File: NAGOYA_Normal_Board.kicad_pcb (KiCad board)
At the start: 2 copper layers, 60 x 71 mm, 104 parts, among them CN1 XT30-M, CN13 value, CN14 RefereeSystem, CN15 micro_B, CN2 XT30-M, CN3 XT30-F, CN4 XT30-F, CN5 XT30-F, CN6 XT30-F, J1 debug, J10 CAN3, J13 CAN3, J14 CAN3, J5 CAN3, J6 CAN3, J7 CAN3, J8 CAN3, J9 CAN3, Q2 DDTC114EUA-7-F, Q4 DDTC114EUA-7-F, Q5 DDTC114EUA-7-F, Q6 DDTC114EUA-7-F, SW1 SW_DIP_x04, U1 Teensy4.1, U2 TCAN1042HVDR, U3 TCAN1042HVDR, U4 TCAN1042HVDR, U5 FT234XD, U6 TLP172AM, U7 BNO055, U8 ADuM121N, U9 LXES11DAA2-137, Y2 32.768 k

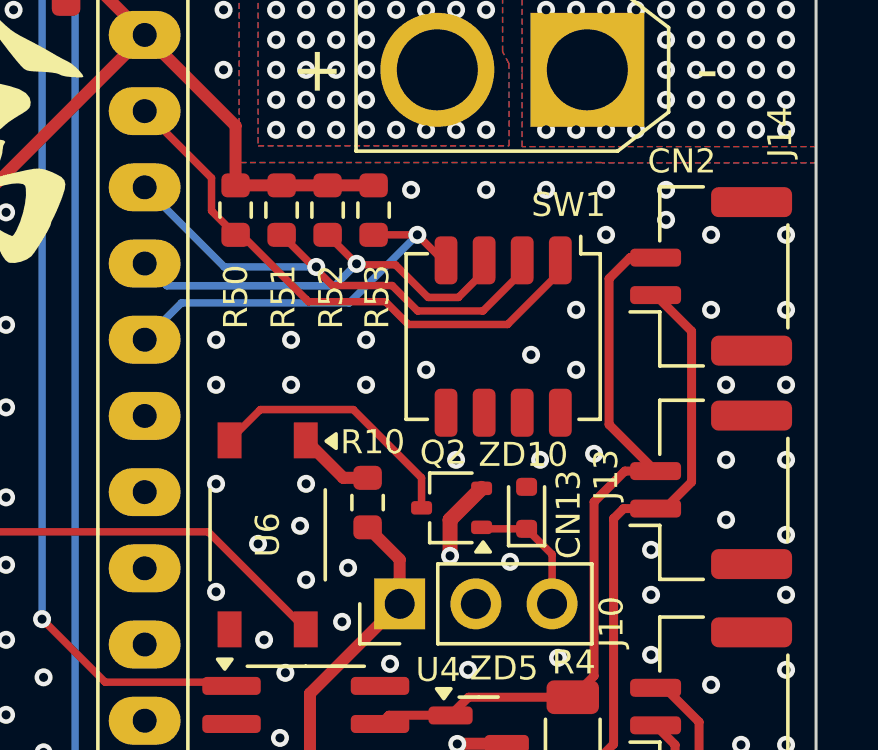
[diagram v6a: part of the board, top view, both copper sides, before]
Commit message: 発注用parameterを変更
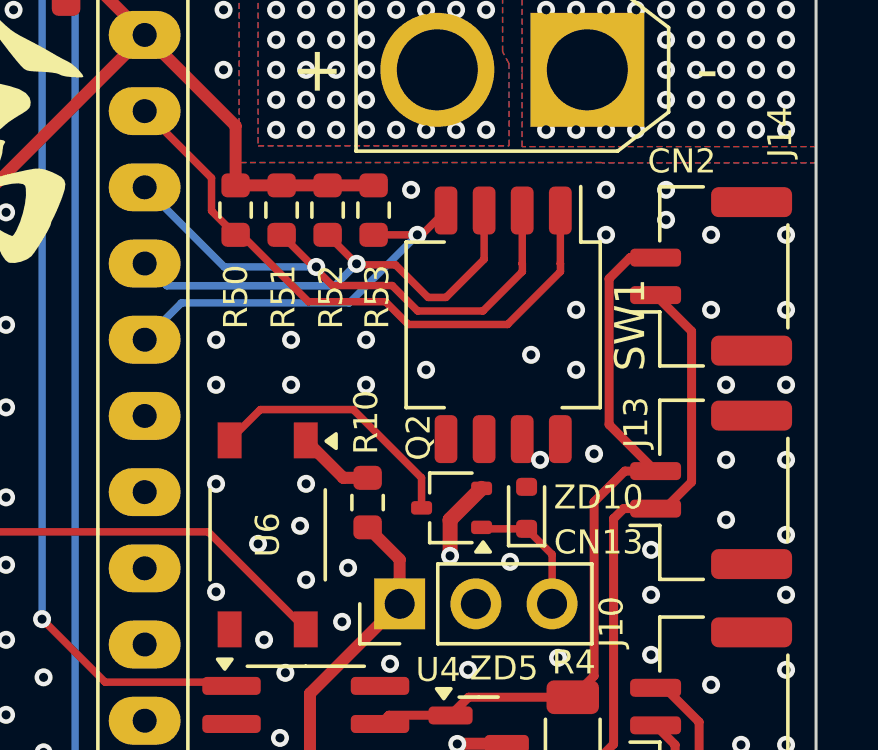
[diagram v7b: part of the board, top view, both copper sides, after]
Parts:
- SW1: footprint Button_Switch_SMD:SW_DIP_SPSTx04_Slide_Copal_CHS-04A_W5.08mm_P1.27mm_JPin -> Button_Switch_SMD:SW_DIP_SPSTx04_Slide_Copal_CHS-04B_W7.62mm_P1.27mm
- moved SW1 0.39 mm to (159.6, 95.5)
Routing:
- net DIP_SW_2: track 16.8 -> 18.5 mm
- net DIP_SW_1: track 18.4 -> 20.2 mm
- net DIP_SW_3: track 14.4 -> 15.9 mm
- net GND: vias 334 -> 331
